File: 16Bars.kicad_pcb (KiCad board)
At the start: 2 copper layers, 28.5 x 105 mm, 40 parts, among them IC1 CD4033BE, IC2 CD4033BE, IC3 CD4510BE, J1 CLOCK_IN, J2 Conn_02x05_Odd_Even, Q1 2N3904, Q2 2N3904, Q3 2N3904, Q4 2N3904, Q5 NPN BJT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

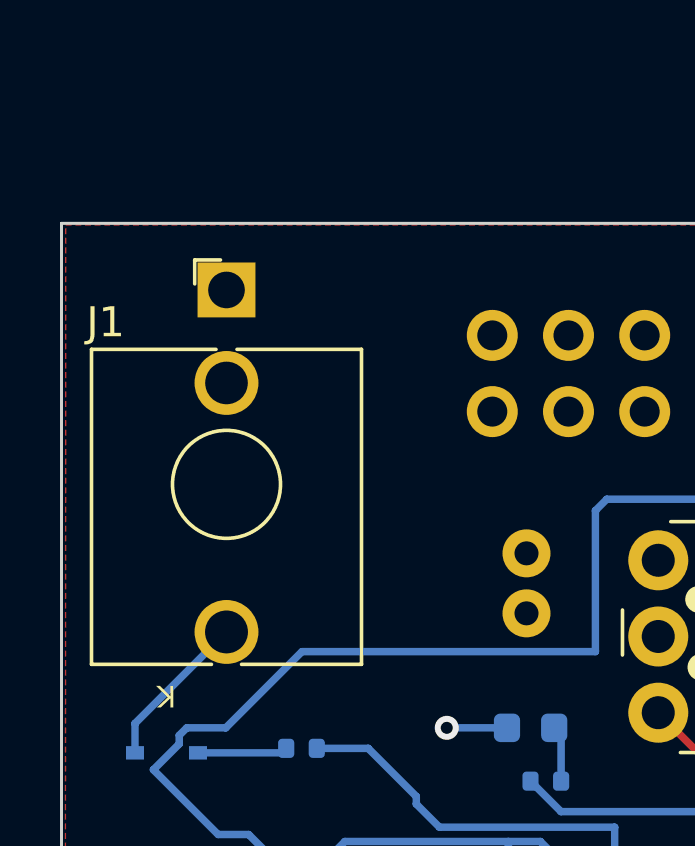
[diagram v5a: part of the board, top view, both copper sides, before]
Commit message: Add 4MS Jack Symbol and Footprint
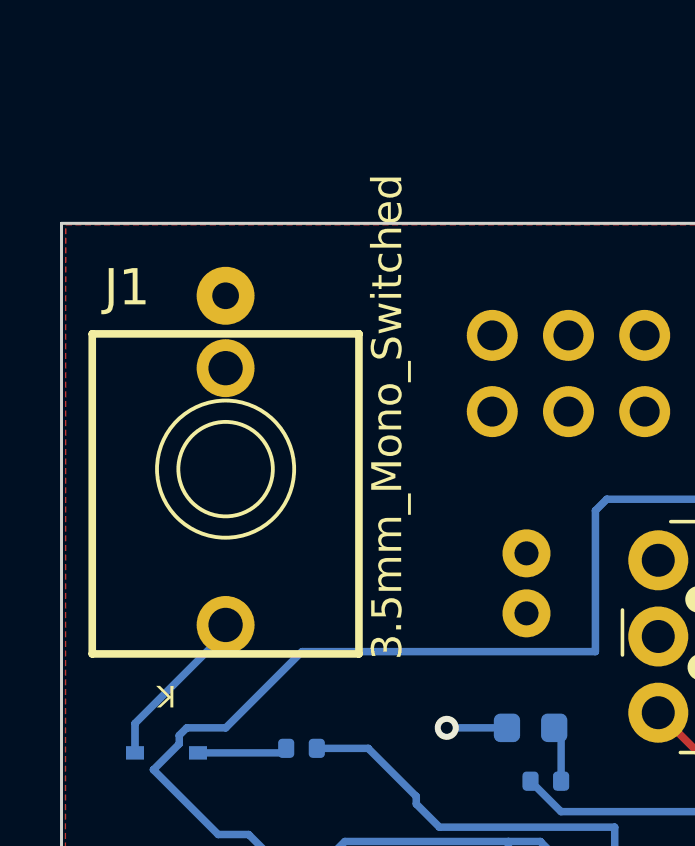
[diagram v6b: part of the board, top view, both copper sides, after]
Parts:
- J1: value CLOCK_IN -> 3.5mm_Mono_Switched; footprint Connector_Audio:Jack_3.5mm_QingPu_WQP-PJ398SM_Vertical_CircularHoles -> 4ms_Jack:EighthInch_PJ398SM
- moved J1 5.96 mm to (62.0, 43.2), turned to 90 degrees
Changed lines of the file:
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@@
   (net 47 "/16_BARS_RESET")
   (net 48 "Net-(IC3-Pad10)")
-  (net 49 "Net-(R11-Pad2)")
+  (net 49 "Net-(Q4-Pad2)")
   (net 50 "Net-(R16-Pad2)")
   (footprint "TDSR*:ThonkLowProfileButton" (layer "F.Cu")
@@
       (scale (xyz 1 1 1))
       (rotate (xyz 0 0 0))
+    )
+  )
+  (footprint "4ms_Jack:EighthInch_PJ398SM" (layer "F.Cu")
+    (at 61.97 43.18 90)
+    (property "Manufacturer" "Wenzhou QingPu Electronics Co")
+    (property "Part Number" "WQP-WQP518MA")
+    (property "Sheetfile" "16Bars.kicad_sch")
+    (property "Sheetname" "")
+    (property "Specifications" "Audio 3.5mm Jack, mono, switched, PC-pin Vertical")
+    (attr through_hole)
+    (fp_text reference "J1" (at 5.334 -4.058 180) (layer "F.SilkS")
+      (effects (font (size 1.2065 1.2065) (thickness 0.1524)) (justify left bottom))
+    )
+    (fp_text value "3.5mm_Mono_Switched" (at -6.375 5.975 90) (layer "F.SilkS")
+      (effects (font (size 1 1) (thickness 0.15)) (justify left bottom))
+    )
+    (fp_line (start 4.4958 -4.445) (end -6.1722 -4.445) (layer "F.SilkS") (width 0.254))
+    (fp_line (start -6.1722 4.445) (end 4.4958 4.445) (layer "F.SilkS") (width 0.254))
+    (fp_line (start -6.1722 -4.445) (end -6.1722 4.445) (layer "F.SilkS") (width 0.254))
+    (fp_line (start 4.4958 4.445) (end 4.4958 -4.445) (layer "F.SilkS") (width 0.254))
+    (fp_circle (center -0.0127 0) (end 1.5621 0) (layer "F.SilkS") (width 0.127) (fill none))
+    (fp_circle (center -0.0127 0) (end 2.2733 0) (layer "F.SilkS") (width 0.127) (fill none))
+    (fp_circle (center 0 0) (end 3.175 0) (layer "Cmts.User") (width 0.0254) (fill none))
+    (fp_line (start -6.44 -4.7) (end -6.44 4.7) (layer "F.CrtYd") (width 0.05))
+    (fp_line (start -6.44 -4.7) (end 4.5 -4.7) (layer "F.CrtYd") (width 0.05))
+    (fp_line (start 4.5 1.16) (end 4.5 4.7) (layer "F.CrtYd") (width 0.05))
+    (fp_line (start -6.44 4.7) (end 4.5 4.7) (layer "F.CrtYd") (width 0.05))
+    (fp_line (start 4.5 -4.7) (end 4.5 -1.16) (layer "F.CrtYd") (width 0.05))
+    (fp_line (start 6.93 1.16) (end 4.5 1.16) (layer "F.CrtYd") (width 0.05))
+    (fp_line (start 6.93 -1.16) (end 6.93 1.16) (layer "F.CrtYd") (width 0.05))
+    (fp_line (start 4.5 -1.16) (end 6.93 -1.16) (layer "F.CrtYd") (width 0.05))
+    (pad "1" thru_hole circle locked (at -5.207 0 90) (size 1.9304 1.9304) (drill 1.143) (layers *.Cu *.Mask)
+      (net 41 "Net-(D1-Pad2)") (pinfunction "SIG") (pintype "passive"))
+    (pad "2" thru_hole circle locked (at 5.7658 0 90) (size 1.9304 1.9304) (drill 0.889) (layers *.Cu *.Mask)
+      (net 6 "GND") (pinfunction "SHEILD") (pintype "passive"))
+    (pad "3" thru_hole circle locked (at 3.3528 0 90) (size 1.9304 1.9304) (drill 1.143) (layers *.Cu *.Mask)
+      (net 6 "GND") (pinfunction "SW") (pintype "passive"))
+    (model "${KICAD_4MS_LIBS}/3dmodels/Jack.3dshapes/PJ301M-12.WRL"
+      (offset (xyz -0.8889999866 0.4063999939 0))
+      (scale (xyz 393 393 393))
+      (rotate (xyz 0 0 -90))
     )
   )
@@
       (net 15 "/F2") (pinfunction "F") (pintype "passive"))
   )
-  (footprint "Connector_Audio:Jack_3.5mm_QingPu_WQP-PJ398SM_Vertical_CircularHoles" (layer "F.Cu")
-    (at 62 37.22)
-    (descr "TRS 3.5mm, vertical, Thonkiconn, PCB mount, (http://www.qingpu-electronics.com/en/products/WQP-PJ398SM-362.html)")
-    (tags "WQP-PJ398SM WQP-PJ301M-12 TRS 3.5mm mono vertical jack thonkiconn qingpu")
-    (property "Sheetfile" "16Bars.kicad_sch")
-    (property "Sheetname" "")
-    (attr through_hole)
-    (fp_text reference "J1" (at -4.03 1.08 180) (layer "F.SilkS")
-      (effects (font (size 1 1) (thickness 0.15)))
-    )
-    (fp_text value "CLOCK_IN" (at 0 5 180) (layer "F.Fab")
-      (effects (font (size 1 1) (thickness 0.15)))
-    )
-    (fp_text user "KEEPOUT" (at 0 6.48) (layer "Cmts.User")
-      (effects (font (size 0.4 0.4) (thickness 0.051)))
-    )
-    (fp_text user "${REFERENCE}" (at 0 8 180) (layer "F.Fab")
-      (effects (font (size 1 1) (thickness 0.15)))
-    )
-    (fp_line (start -0.5 12.48) (end -4.5 12.48) (layer "F.SilkS") (width 0.12))
-    (fp_line (start -4.5 1.98) (end -4.5 12.48) (layer "F.SilkS") (width 0.12))
-    (fp_line (start 4.5 12.48) (end 0.5 12.48) (layer "F.SilkS") (width 0.12))
-    (fp_line (start -1.06 -1) (end -0.2 -1) (layer "F.SilkS") (width 0.12))
-    (fp_line (start -1.06 -1) (end -1.06 -0.2) (layer "F.SilkS") (width 0.12))
-    (fp_line (start -0.35 1.98) (end -4.5 1.98) (layer "F.SilkS") (width 0.12))
-    (fp_line (start 4.5 1.98) (end 4.5 12.48) (layer "F.SilkS") (width 0.12))
-    (fp_line (start 4.5 1.98) (end 0.35 1.98) (layer "F.SilkS") (width 0.12))
-    (fp_circle (center 0 6.48) (end 1.8 6.48) (layer "F.SilkS") (width 0.12) (fill none))
-    (fp_line (start 0.09 7.96) (end 1.48 6.57) (layer "Dwgs.User") (width 0.12))
-    (fp_line (start -1.42 6.875) (end 0.4 5.06) (layer "Dwgs.User") (width 0.12))
-    (fp_line (start -1.07 7.49) (end 1.01 5.41) (layer "Dwgs.User") (width 0.12))
-    (fp_line (start -0.58 7.83) (end 1.36 5.89) (layer "Dwgs.User") (width 0.12))
-    (fp_line (start -1.41 6.02) (end -0.46 5.07) (layer "Dwgs.User") (width 0.12))
-    (fp_circle (center 0 6.48) (end 1.5 6.48) (layer "Dwgs.User") (width 0.12) (fill none))
-    (fp_line (start 5 12.98) (end 5 -1.42) (layer "F.CrtYd") (width 0.05))
-    (fp_line (start 5 12.98) (end -5 12.98) (layer "F.CrtYd") (width 0.05))
-    (fp_line (start -5 12.98) (end -5 -1.42) (layer "F.CrtYd") (width 0.05))
-    (fp_line (start 5 -1.42) (end -5 -1.42) (layer "F.CrtYd") (width 0.05))
-    (fp_line (start 0 0) (end 0 2.03) (layer "F.Fab") (width 0.1))
-    (fp_line (start 4.5 2.03) (end -4.5 2.03) (layer "F.Fab") (width 0.1))
-    (fp_line (start 4.5 12.48) (end 4.5 2.08) (layer "F.Fab") (width 0.1))
-    (fp_line (start 4.5 12.48) (end -4.5 12.48) (layer "F.Fab") (width 0.1))
-    (fp_line (start -4.5 12.48) (end -4.5 2.08) (layer "F.Fab") (width 0.1))
-    (fp_circle (center 0 6.48) (end 1.8 6.48) (layer "F.Fab") (width 0.1) (fill none))
-    (pad "S" thru_hole rect (at 0 0 180) (size 1.93 1.83) (drill 1.22) (layers *.Cu *.Mask)
-      (net 6 "GND") (pintype "passive"))
-    (pad "T" thru_hole circle (at 0 11.4 180) (size 2.13 2.13) (drill 1.43) (layers *.Cu *.Mask)
-      (net 41 "Net-(D1-Pad2)") (pintype "passive"))
-    (pad "TN" thru_hole circle (at 0 3.1 180) (size 2.13 2.13) (drill 1.42) (layers *.Cu *.Mask))
-    (model "${KICAD6_3DMODEL_DIR}/Connector_Audio.3dshapes/Jack_3.5mm_QingPu_WQP-PJ398SM_Vertical.wrl"
-      (offset (xyz 0 0 0))
-      (scale (xyz 1 1 1))
-      (rotate (xyz 0 0 0))
-    )
-  )
   (footprint "MountingHole:MountingHole_3.2mm_M3" (layer "F.Cu")
     (at 70.5 121)
@@
       (net 1 "/E1") (pintype "passive"))
     (pad "2" smd roundrect (at 0.51 0 180) (size 0.54 0.64) (layers "B.Cu" "B.Paste" "B.Mask") (roundrect_rratio 0.25)
-      (net 49 "Net-(R11-Pad2)") (pintype "passive"))
+      (net 49 "Net-(Q4-Pad2)") (pintype "passive"))
     (model "${KICAD6_3DMODEL_DIR}/Resistor_SMD.3dshapes/R_0402_1005Metric.wrl"
       (offset (xyz 0 0 0))
@@
       (net 6 "GND") (pinfunction "E") (pintype "passive"))
     (pad "2" smd custom (at -1.5625 0 270) (size 1.475 0.9) (layers "B.Cu" "B.Paste" "B.Mask")
-      (net 49 "Net-(R11-Pad2)") (pinfunction "B") (pintype "passive") (zone_connect 2)
+      (net 49 "Net-(Q4-Pad2)") (pinfunction "B") (pintype "passive") (zone_connect 2)
       (options (clearance outline) (anchor rect))
       (primitives
